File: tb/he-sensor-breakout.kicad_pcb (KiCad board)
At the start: 2 copper layers, 19.1 x 29.1 mm, 35 parts, among them J1 Conn_01x01_Pin, J10 Conn_01x01_Pin, J11 Conn_01x01_Pin, J12 Conn_01x01_Pin, J13 Conn_01x01_Pin, J14 Conn_01x01_Pin, J2 Conn_01x01_Pin, J3 Conn_01x01_Pin, J4 Conn_01x01_Pin, J5 Conn_01x01_Pin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

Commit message: finishing touches
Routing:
- net VDDA: track 22.3 -> 23.0 mm
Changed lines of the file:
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@@
   (segment (start 102.05 98.5) (end 102.05 98.592933) (width 0.5) (layer "B.Cu") (net 1))
   (segment (start 92.82 94.92) (end 92.38 94.92) (width 0.5) (layer "F.Cu") (net 2))
+  (segment (start 97.75 97.95) (end 97.75 100.13) (width 0.5) (layer "B.Cu") (net 2))
+  (segment (start 102.25 99.903961) (end 101.153961 101) (width 0.5) (layer "B.Cu") (net 2))
+  (segment (start 99.407067 101) (end 98.8625 100.455433) (width 0.5) (layer "B.Cu") (net 2))
+  (segment (start 94.72 94.92) (end 97.75 97.95) (width 0.5) (layer "B.Cu") (net 2))
+  (segment (start 101.153961 101) (end 99.407067 101) (width 0.5) (layer "B.Cu") (net 2))
+  (segment (start 102.25 99.875) (end 102.25 99.903961) (width 0.5) (layer "B.Cu") (net 2))
+  (segment (start 98.015433 100.455433) (end 97.72 100.16) (width 0.5) (layer "B.Cu") (net 2))
+  (segment (start 97.75 100.13) (end 97.72 100.16) (width 0.5) (layer "B.Cu") (net 2))
+  (segment (start 98.8625 100.455433) (end 98.015433 100.455433) (width 0.5) (layer "B.Cu") (net 2))
   (segment (start 107.205 94.92) (end 102.25 99.875) (width 0.5) (layer "B.Cu") (net 2))
+  (segment (start 96.825 100.05) (end 97.61 100.05) (width 0.5) (layer "B.Cu") (net 2))
+  (segment (start 97.61 100.05) (end 97.72 100.16) (width 0.5) (layer "B.Cu") (net 2))
   (segment (start 92.38 94.92) (end 94.72 94.92) (width 0.5) (layer "B.Cu") (net 2))
-  (segment (start 97.75 99.436683) (end 97.84375 99.436683) (width 0.5) (layer "B.Cu") (net 2))
-  (segment (start 102.25 99.903961) (end 101.698528 100.455433) (width 0.5) (layer "B.Cu") (net 2))
-  (segment (start 101.698528 100.455433) (end 98.8625 100.455433) (width 0.5) (layer "B.Cu") (net 2))
-  (segment (start 97.84375 99.436683) (end 98.8625 100.455433) (width 0.5) (layer "B.Cu") (net 2))
-  (segment (start 97.75 97.95) (end 97.75 99.436683) (width 0.5) (layer "B.Cu") (net 2))
-  (segment (start 94.72 94.92) (end 97.75 97.95) (width 0.5) (layer "B.Cu") (net 2))
-  (segment (start 97.75 99.436683) (end 97.136683 100.05) (width 0.5) (layer "B.Cu") (net 2))
-  (segment (start 102.25 99.875) (end 102.25 99.903961) (width 0.5) (layer "B.Cu") (net 2))
   (segment (start 107.62 94.92) (end 107.205 94.92) (width 0.5) (layer "B.Cu") (net 2))
-  (segment (start 97.136683 100.05) (end 96.825 100.05) (width 0.5) (layer "B.Cu") (net 2))
   (via (at 94.488188 104.938188) (size 0.8) (drill 0.4) (layers "F.Cu" "B.Cu") (free) (net 3))
   (via (at 102.3 106.375) (size 0.8) (drill 0.4) (layers "F.Cu" "B.Cu") (free) (net 3))
@@
   (segment (start 105.225 101.775) (end 105.825 101.175) (width 0.5) (layer "B.Cu") (net 3))
   (segment (start 94.288317 103.936683) (end 95.4 103.936683) (width 0.5) (layer "B.Cu") (net 4))
-  (segment (start 97.5 103.487664) (end 97.5 103.925) (width 0.5) (layer "B.Cu") (net 4))
+  (segment (start 98.37 102.4) (end 97.5 103.27) (width 0.5) (layer "B.Cu") (net 4))
   (segment (start 93.145 105.08) (end 94.288317 103.936683) (width 0.5) (layer "B.Cu") (net 4))
   (segment (start 95.4 103.936683) (end 97.488317 103.936683) (width 0.5) (layer "B.Cu") (net 4))
+  (segment (start 97.5 103.27) (end 97.5 103.925) (width 0.5) (layer "B.Cu") (net 4))
+  (segment (start 105.865 103.325) (end 104.185051 103.325) (width 0.5) (layer "B.Cu") (net 4))
+  (segment (start 97.488317 103.936683) (end 97.5 103.925) (width 0.5) (layer "B.Cu") (net 4))
   (segment (start 107.62 105.08) (end 105.865 103.325) (width 0.5) (layer "B.Cu") (net 4))
-  (segment (start 98.587664 102.4) (end 97.5 103.487664) (width 0.5) (layer "B.Cu") (net 4))
-  (segment (start 97.488317 103.936683) (end 97.5 103.925) (width 0.5) (layer "B.Cu") (net 4))
-  (segment (start 105.865 103.325) (end 104.185051 103.325) (width 0.5) (layer "B.Cu") (net 4))
-  (segment (start 103.260051 102.4) (end 98.587664 102.4) (width 0.5) (layer "B.Cu") (net 4))
   (segment (start 104.185051 103.325) (end 103.260051 102.4) (width 0.5) (layer "B.Cu") (net 4))
+  (segment (start 103.260051 102.4) (end 98.37 102.4) (width 0.5) (layer "B.Cu") (net 4))
   (segment (start 92.38 105.08) (end 93.145 105.08) (width 0.5) (layer "B.Cu") (net 4))
   (segment (start 95.825 108.525) (end 94.92 107.62) (width 0.3) (layer "B.Cu") (net 5))
@@
         (xy 91.474749 100.412665)
         (xy 95.224749 100.437665)
-        (xy 97.699749 102.137665)
-        (xy 103.224749 102.137665)
-        (xy 105.599749 100.437665)
-        (xy 108.724749 100.462665)
+        (xy 97.59 102.04)
+        (xy 102.58 101.97)
+        (xy 104.81 100.49)
+        (xy 108.724749 100.375)
         (xy 108.799749 103.912665)
         (xy 108.749749 103.987665)
         (xy 108.649749 106.462665)
         (xy 108.749749 106.762665)
-        (xy 108.675 108.925)
-        (xy 91.175 108.937665)
+        (xy 108.655 108.995)
+        (xy 91.155 109.007665)
         (xy 91.124749 106.587665)
         (xy 91.35 100.725)

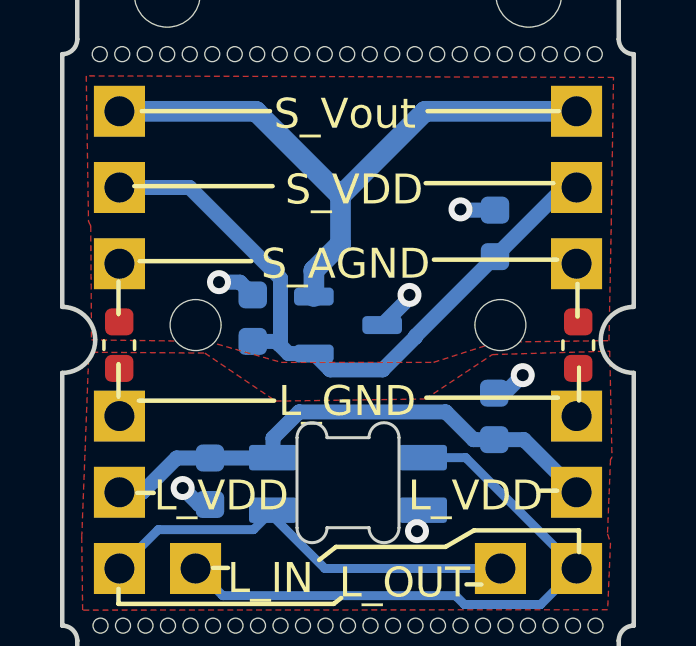
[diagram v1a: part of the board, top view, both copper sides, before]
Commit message: adds vdd and vdd connection pads
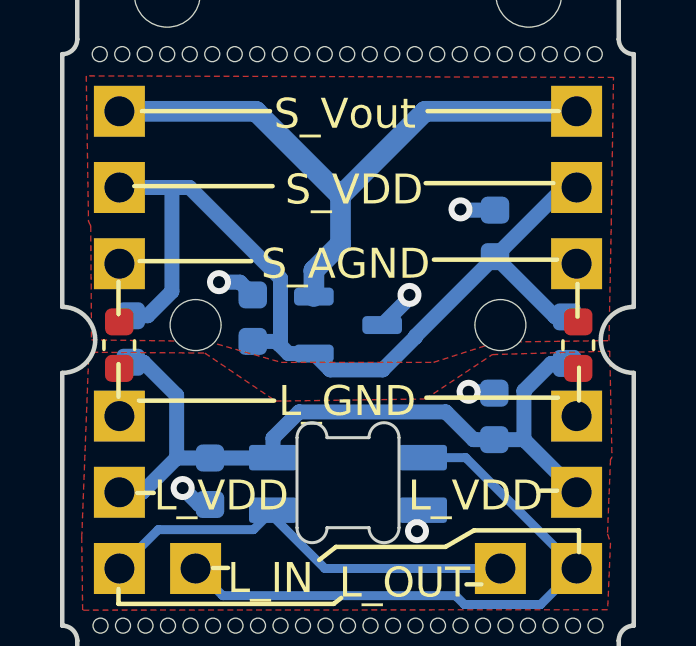
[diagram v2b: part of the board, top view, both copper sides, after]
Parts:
- added R3: R, Capacitor_SMD:C_0603_1608Metric, B.Cu at (107.3, 100.0)
- added R4: R, Capacitor_SMD:C_0603_1608Metric, B.Cu at (92.8, 100.0)
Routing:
- net VDDA: track 23.0 -> 31.4 mm
- net VDD: track 17.8 -> 25.4 mm

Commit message: vdda and vdd connection
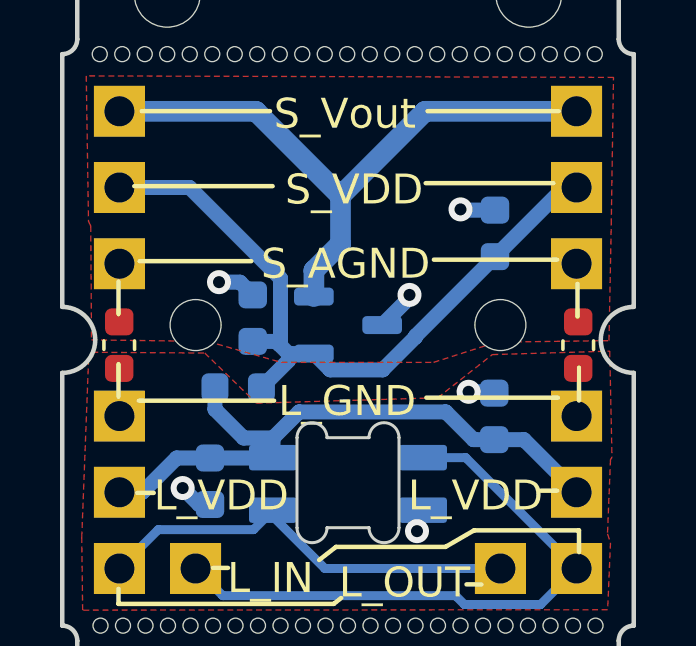
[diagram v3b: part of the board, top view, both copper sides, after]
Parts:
- removed R4: R, Capacitor_SMD:C_0603_1608Metric
- moved R3 11.1 mm to (96.3, 101.6), turned to 0 degrees
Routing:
- net VDDA: track 31.4 -> 24.5 mm
- net VDD: track 25.4 -> 20.9 mm

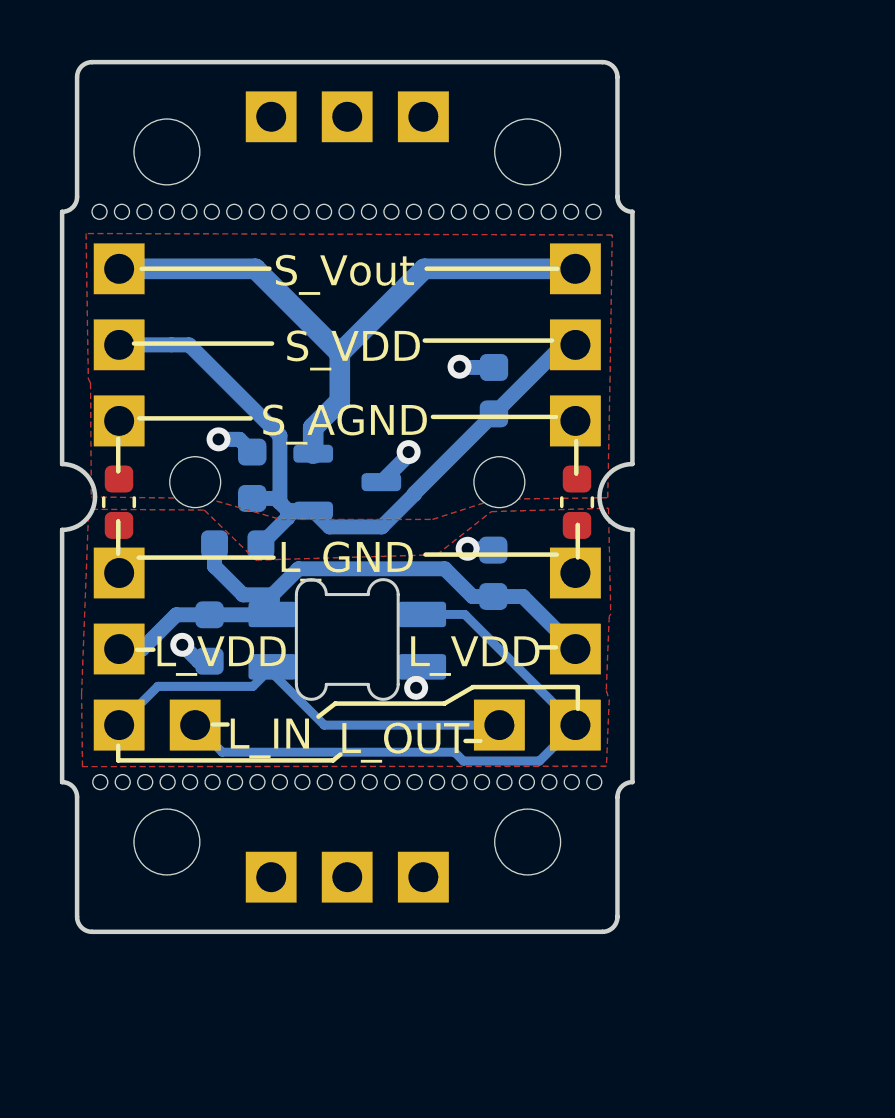
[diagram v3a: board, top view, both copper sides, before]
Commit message: moves holes and adds silkscreen
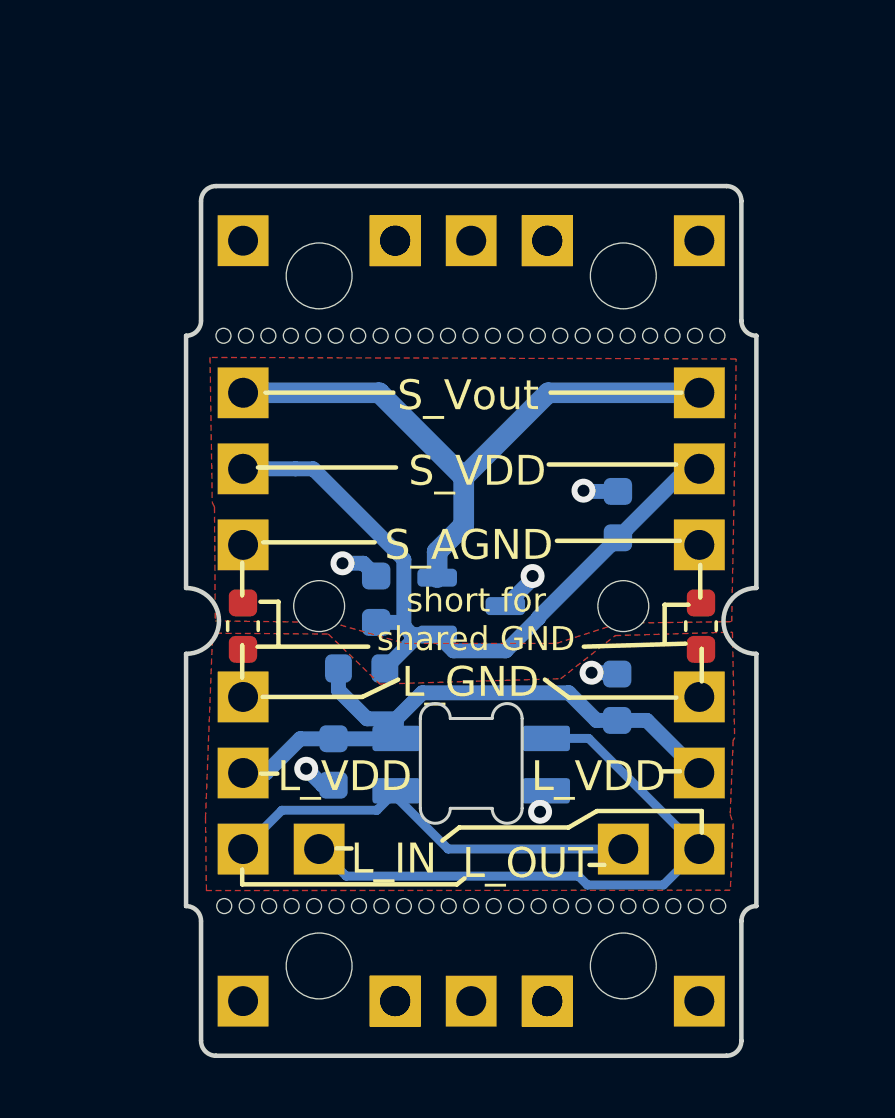
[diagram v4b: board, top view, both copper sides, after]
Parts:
- added ? (x2): , , F.Cu at (101.6, 91.4)
- added ? (x2): , , F.Cu at (101.6, 116.8)
- added ? (x2): , , F.Cu at (106.7, 91.4)
- added ? (x2): , , F.Cu at (106.7, 116.8)
- moved ? 10.1 mm to (111.8, 91.4)
- moved ? 10.1 mm to (111.8, 116.8)
- moved H1 6.56 mm to (99.1, 92.6)
- moved H1 6.56 mm to (99.1, 115.7)
- moved ? 5.85 mm to (104.1, 116.8)
- moved ? 5.85 mm to (104.1, 91.4)
- moved C1 5.85 mm to (99.5, 108.9)
- moved C2 5.85 mm to (109.0, 106.7)
- moved C3 5.85 mm to (109.0, 100.6)
- moved C4 5.85 mm to (101.0, 103.4)
- moved D1 5.85 mm to (104.1, 108.9)
- moved J1 5.85 mm to (111.8, 109.2)
- moved J10 5.85 mm to (96.5, 96.5)
- moved J11 5.85 mm to (109.2, 111.8)
- moved J12 5.85 mm to (96.5, 111.8)
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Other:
- board text added: "LGND"
- board text added: "Short back pads to share VDD"
- board text added: "short for shared GND"

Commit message: move tabs
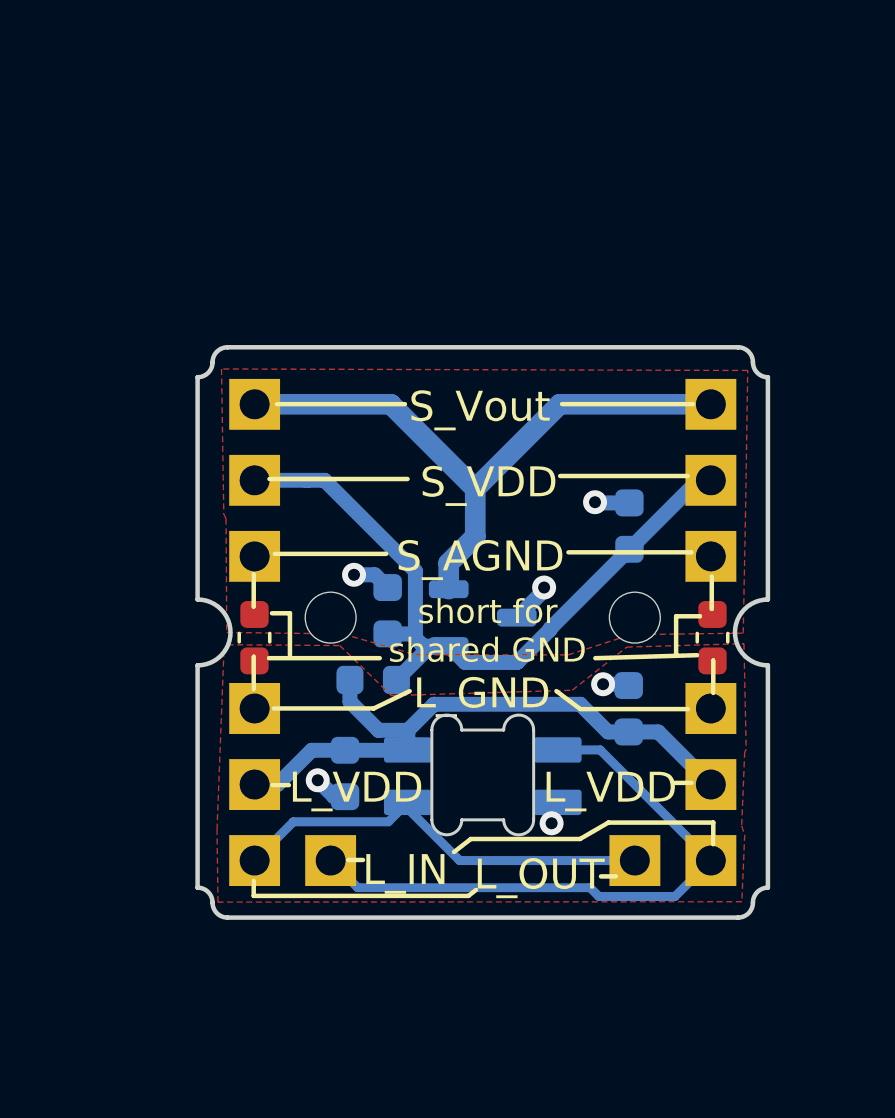
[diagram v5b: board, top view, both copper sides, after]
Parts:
- removed ? (x14): , 
- removed H1 (x2), H2 (x2): MountingHole_2.2mm_M2, MountingHole:MountingHole_2.2mm_M2
- removed MOUSE1, MOUSE2: mouse-bite-19mm, Panelization:mouse-bite-19mm
- moved C2 0.54 mm to (109.4, 107.1)
- moved D1 0.54 mm to (104.5, 109.3)
- moved J10 0.54 mm to (96.9, 96.9)
- moved J2 0.54 mm to (96.9, 109.6)
- moved J3 0.54 mm to (96.9, 102.0)
- moved R1 0.54 mm to (112.2, 104.7)
- moved R2 0.54 mm to (96.9, 104.7)
- moved SW 0.54 mm to (104.5, 104.0)
- moved U1 0.54 mm to (104.5, 104.0)
- moved C1 0.54 mm to (99.9, 109.2)
- moved J1 0.54 mm to (112.1, 109.6)
- moved J11 0.54 mm to (109.6, 112.1)
- moved J12 0.54 mm to (96.9, 112.1)
- moved J4 0.54 mm to (112.1, 102.0)
- moved J5 0.54 mm to (96.9, 99.4)
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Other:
- board size 19.1 x 29.1 mm -> 19 x 19 mm
- board text removed: "Short back pads to share VDD"

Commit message: moves GND shorts
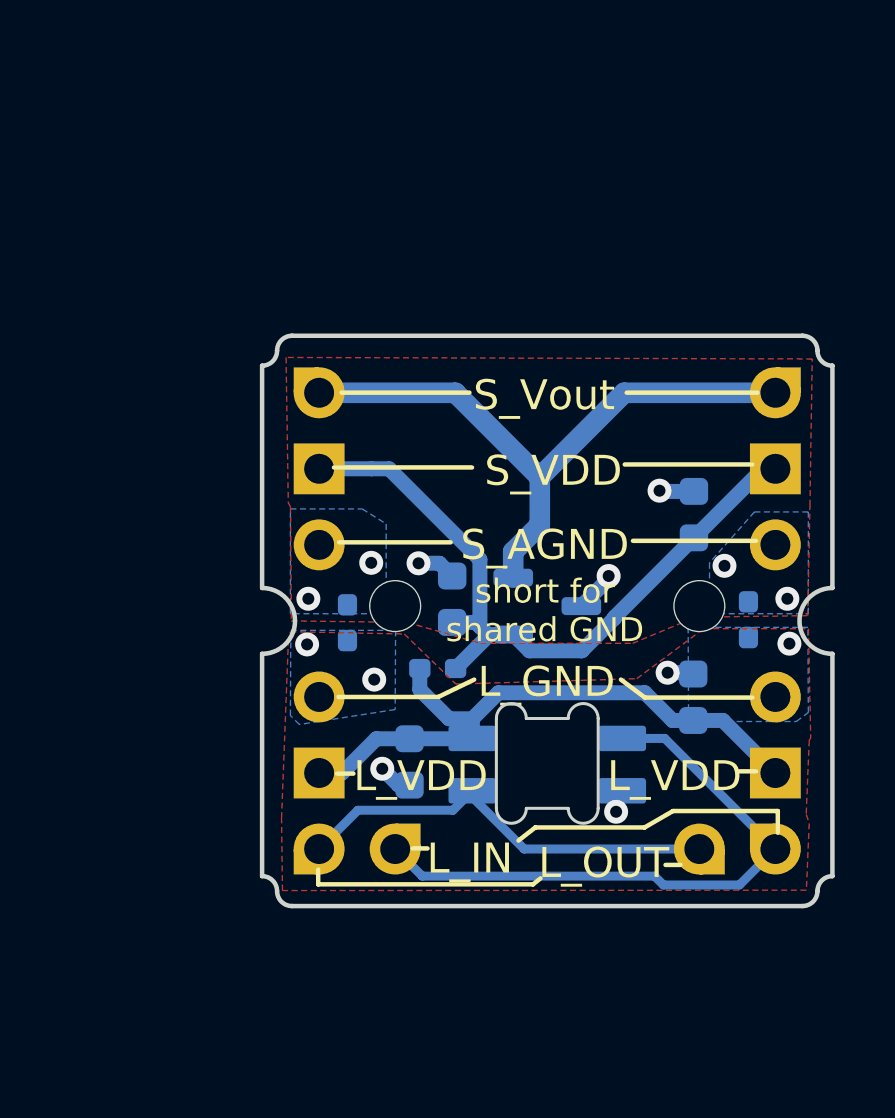
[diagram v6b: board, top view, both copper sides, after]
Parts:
- R1, R2: footprint Capacitor_SMD:C_0603_1608Metric -> Resistor_SMD:R_0402_1005Metric_Pad0.72x0.64mm_HandSolder; moved to B.Cu
- R3: footprint Capacitor_SMD:C_0603_1608Metric -> Resistor_SMD:R_0402_1005Metric_Pad0.72x0.64mm_HandSolder
- moved R2 3.15 mm to (100.0, 104.2)
- moved C1 2.19 mm to (102.1, 108.9)
- moved C2 2.19 mm to (111.6, 106.7)
- moved D1 2.19 mm to (106.7, 108.9)
- moved J1 2.19 mm to (114.3, 109.2)
- moved J10 2.19 mm to (99.1, 96.5)
- moved J2 2.19 mm to (99.1, 109.2)
- moved J3 2.19 mm to (99.1, 101.6)
- moved J4 2.19 mm to (114.3, 101.6)
- moved J9 2.19 mm to (114.3, 96.5), turned to 90 degrees
- moved SW 2.19 mm to (106.7, 103.6)
- moved U1 2.19 mm to (106.7, 103.6)
- moved C3 2.19 mm to (111.6, 100.6)
- moved C4 2.19 mm to (103.5, 103.4)
- moved J11 2.19 mm to (111.8, 111.8), turned to 0 degrees
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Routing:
- net GNDA: vias 3 -> 7
- net GNDD: vias 3 -> 6
- added copper zone on B.Cu, net GNDA
- added copper zone on B.Cu, net GNDD
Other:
- board size 19 x 19 mm -> 19 x 19.1 mm
- board text removed: "LGND"

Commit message: changes hole sizes to m1.6
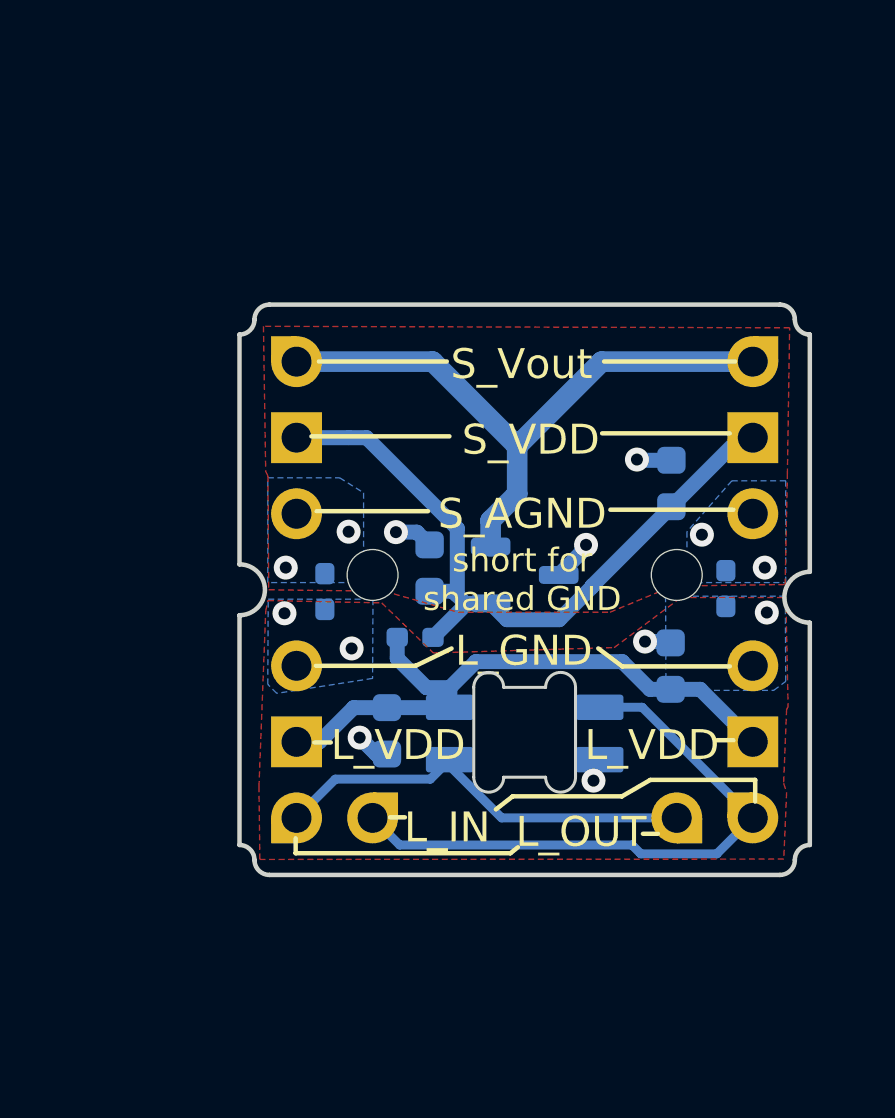
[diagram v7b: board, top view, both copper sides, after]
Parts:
- moved J11 1.29 mm to (111.0, 110.7)
- moved R2 1.29 mm to (99.3, 103.2)
- moved C3 1.29 mm to (110.8, 99.5)
- moved C4 1.29 mm to (102.8, 102.4)
- moved J12 1.29 mm to (98.3, 110.7)
- moved J13 1.29 mm to (100.8, 110.7)
- moved J14 1.29 mm to (113.5, 110.7)
- moved J5 1.29 mm to (98.3, 98.0)
- moved J6 1.29 mm to (113.5, 98.0)
- moved J7 1.29 mm to (113.5, 105.6)
- moved J8 1.29 mm to (98.3, 105.6)
- moved R3 1.29 mm to (102.3, 104.7)
- moved C2 1.29 mm to (110.8, 105.7)
- moved D1 1.29 mm to (105.9, 107.9)
- moved R1 1.29 mm to (112.6, 103.1)
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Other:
- board size 19 x 19.1 mm -> 19 x 19 mm
